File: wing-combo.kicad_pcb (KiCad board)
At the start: 2 copper layers, 91.3 x 91.3 mm, 120 parts, among them J1 Screw_Terminal_01x06, J13 USB_A, J15 Conn_01x16, J16 Conn_01x16, J17 Screw_Terminal_01x06, J18 Screw_Terminal_01x06, J3 Conn_01x12, J4 Conn_01x12, J5 USB_C_Receptacle_USB2.0_16P, T1 AO3400A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

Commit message: ordered B1P3 test run from JLCPCB
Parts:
- D3, D4: value B160-E3 -> SS14
- moved JP18 3.58 mm to (75.5, 65.1)
- moved JP19 3.58 mm to (75.5, 61.5)
- turned R7 to 180 degrees
- turned R8 to 180 degrees
- renumbered IN-1 to J6, IN-2 to J7, IN-3 to J8
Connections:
- JP18 pad 1: Net-(JP18-A) -> SCL
- JP18 pad 2: +3.3V -> Net-(JP18-B)
- JP19 pad 1: Net-(JP19-A) -> SDA
- JP19 pad 2: +3.3V -> Net-(JP19-B)
- R7 pad 1: SDA -> Net-(JP19-B)
- R7 pad 2: Net-(JP19-A) -> +3.3V
- R8 pad 1: SCL -> Net-(JP18-B)
- R8 pad 2: Net-(JP18-A) -> +3.3V
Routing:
- net SDA: track 105.2 -> 134.0 mm, vias 3 -> 4
- net Net-(JP18-A): track 25.8 -> 0.00 mm, vias 1 -> 0
- net Net-(JP19-B): track 0.00 -> 23.2 mm, vias 0 -> 1
- net Net-(JP19-A): track 20.5 -> 0.00 mm, vias 1 -> 0
- net Net-(JP18-B): track 0.00 -> 20.5 mm, vias 0 -> 1
- net SCL: track 105.4 -> 125.5 mm, vias 4 -> 6
- net +3.3V: track 221.0 -> 210.9 mm, vias 9 -> 11
- net set3v: track 41.8 -> 41.1 mm
- net GND: vias 22 -> 20

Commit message: cleanup
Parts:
- removed R29, R36: 1k, Resistor_SMD:R_0603_1608Metric
- removed R30, R37: 10k, Resistor_SMD:R_0603_1608Metric
- removed T7: AO3400A, Package_TO_SOT_SMD:SOT-23
- added R40: 1k, Resistor_SMD:R_0603_1608Metric, F.Cu at (76.0, 71.0)
- added U1: 74HC02, 74hc02d:SOIC-14_L8.7-W3.9-P1.27-LS6.0-BL, F.Cu at (56.8, 50.5)
- moved R28 40.0 mm to (51.5, 47.6), turned to 90 degrees
- moved T1 15.6 mm to (46.6, 66.4), turned to 180 degrees
- moved R2 13.9 mm to (50.3, 64.6), turned to 0 degrees
- moved R33 10.5 mm to (47.9, 40.0), turned to 90 degrees
- moved R32 9.43 mm to (60.1, 39.8), turned to 90 degrees
- moved R1 7.27 mm to (51.5, 50.8), turned to -90 degrees
- moved F2 1.50 mm to (97.4, 27.9)
- moved R27 0.13 mm to (73.3, 86.5)
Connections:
- net /mainslevelcontrol/stage1relays/dcp2 renamed Net-(D4-A)
- R27 pad 1: set3v -> Net-(R27-Pad1)
- R27 pad 2: Net-(T3-G) -> Net-(T7-G)
- R28 pad 1: Net-(T3-G) -> GND
- R28 pad 2: GND -> read-bypass
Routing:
- net Net-(D3-A): track 74.0 -> 11.1 mm, vias 1 -> 0
- net Net-(R27-Pad1): track 0.00 -> 55.7 mm, vias 0 -> 4
- net Net-(R40-Pad1): track 0.00 -> 39.9 mm, vias 0 -> 4
- net set3v: track 41.1 -> 9.19 mm, vias 1 -> 0
- net +3.3V: track 210.9 -> 231.6 mm
- net read-bypass: track 41.3 -> 58.5 mm
- net reset3v: track 26.6 -> 12.3 mm, vias 1 -> 0
- net /microcontroller/lightsounds/dcp1: track 20.8 -> 7.44 mm
- net GND: track 112.0 -> 99.6 mm, vias 20 -> 21
- net Net-(T3-G): track 12.2 -> 1.80 mm
- net Net-(T7-G): track 10.2 -> 0.00 mm
- net Net-(T1-G): track 8.06 -> 18.2 mm
- net buzz: track 6.08 -> 14.8 mm, vias 0 -> 2
- net SDA: track 134.0 -> 130.6 mm, vias 4 -> 5
- net Net-(T4-G): track 7.32 -> 4.67 mm
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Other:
- board text removed: "MAX4A Fuses 5x20mm"

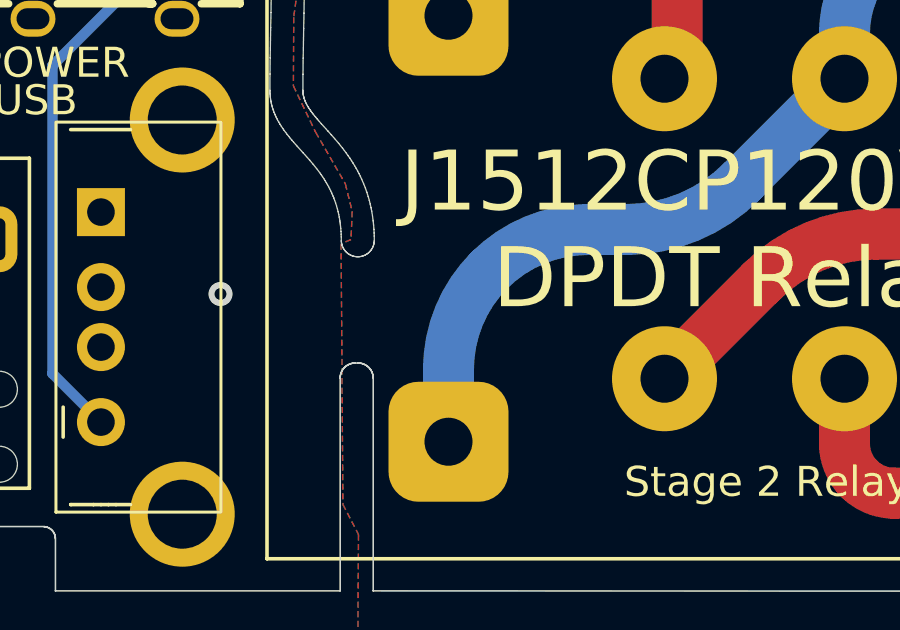
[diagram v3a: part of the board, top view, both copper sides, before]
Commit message: changed to py14-02 relay socket
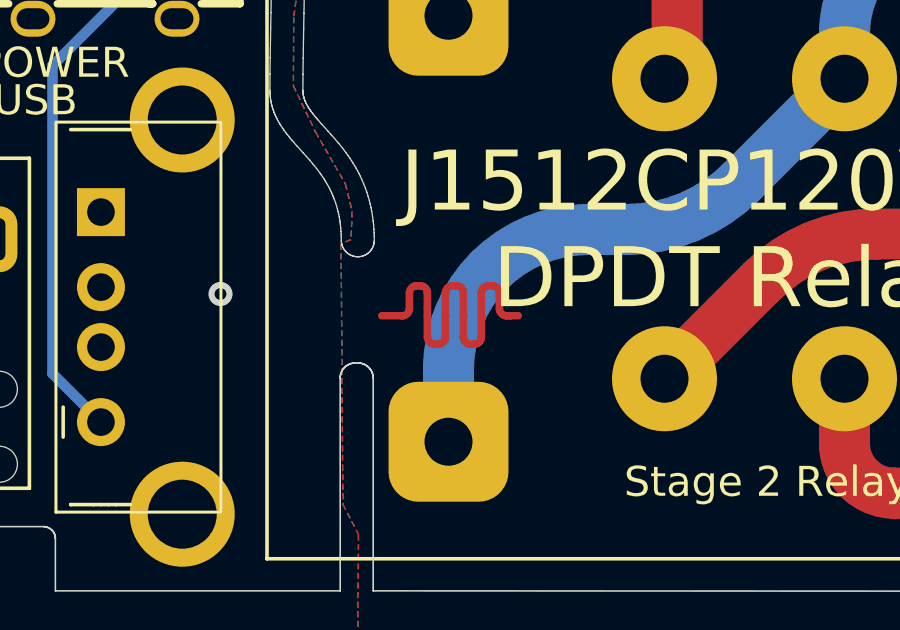
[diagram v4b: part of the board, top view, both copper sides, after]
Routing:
- net (no net): track 0.00 -> 13.0 mm
